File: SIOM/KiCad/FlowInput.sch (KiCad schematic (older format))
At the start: 11 parts, among them Q301 BSS138, Q302 BSS138

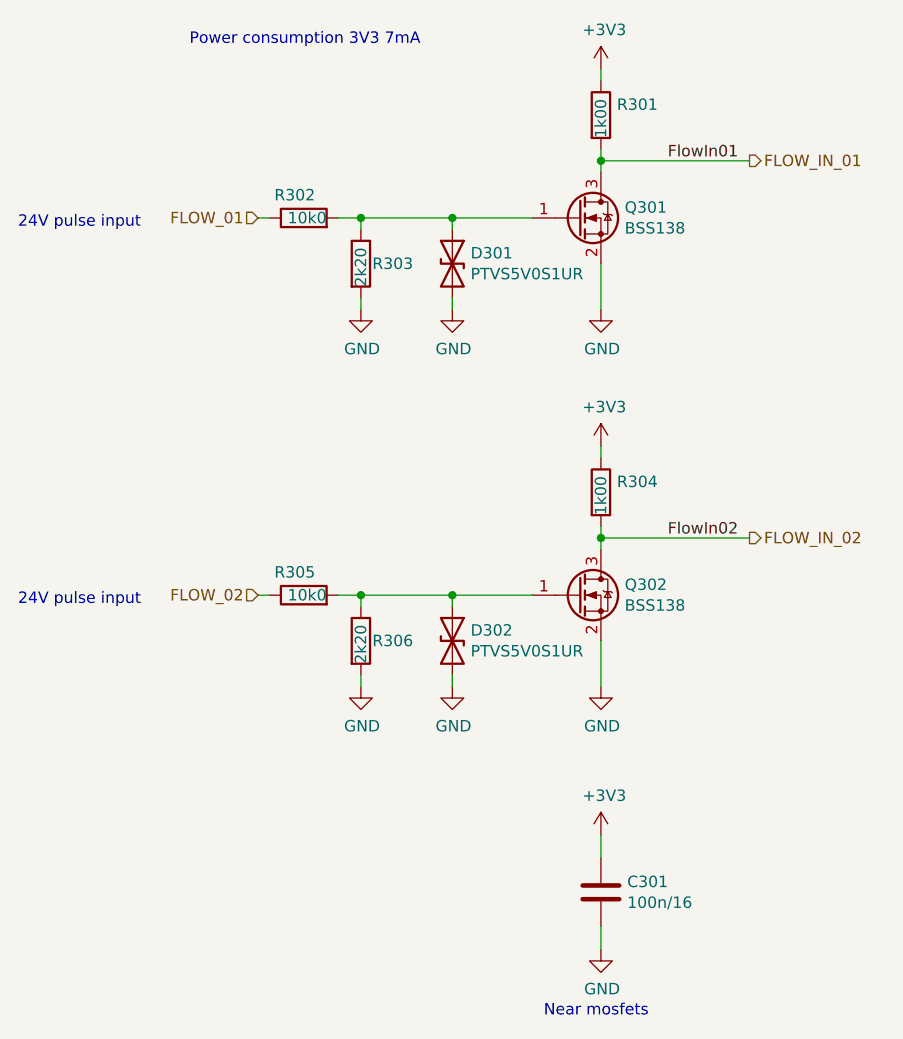
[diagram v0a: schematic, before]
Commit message: KiCad files SIOM_def
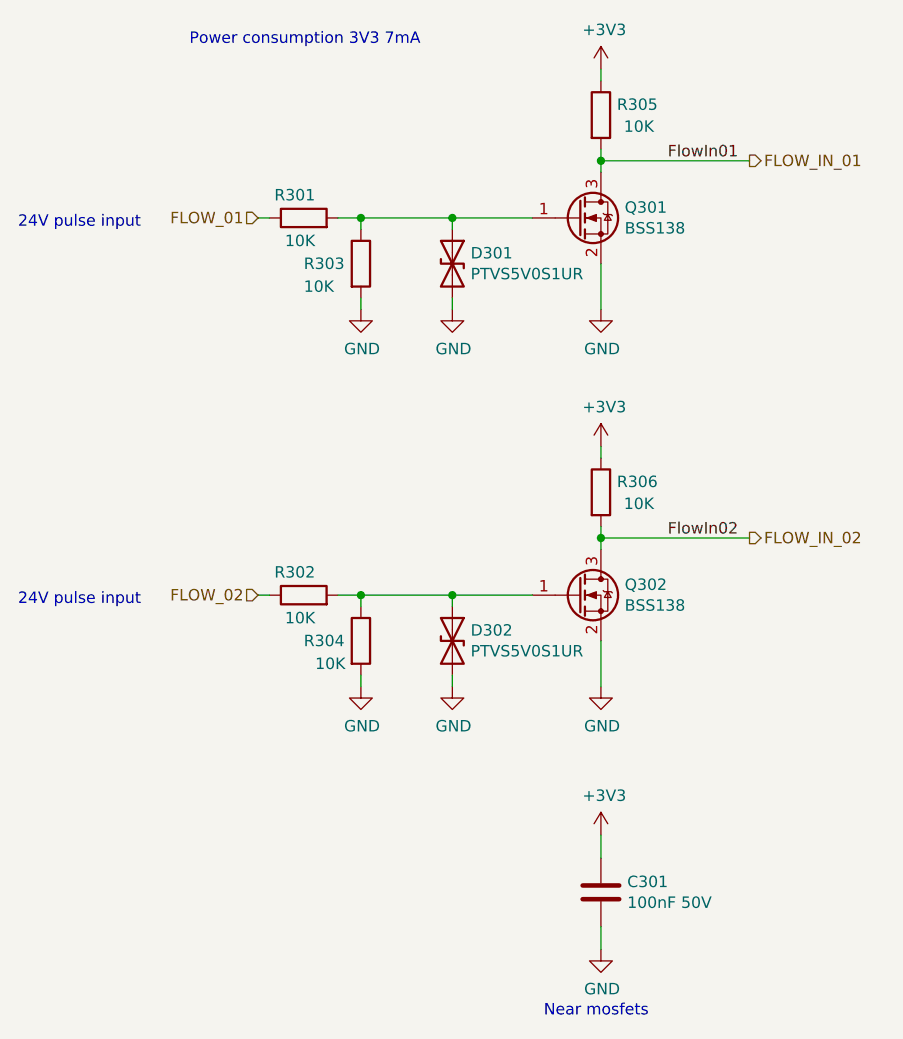
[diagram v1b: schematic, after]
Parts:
- C301: value 100n/16 -> 100nF 50V
- D301, D302: footprint Diode_SMD:Nexperia_CFP3_SOD-123W -> Diode_SMD:D_SOD-123
- R301: renamed from R302; value 10k0 -> 10K
- R302: renamed from R305; value 10k0 -> 10K
- R303: value 2k20 -> 10K
- R304: renamed from R306; value 2k20 -> 10K
- R305: renamed from R301; value 1k00 -> 10K
- R306: renamed from R304; value 1k00 -> 10K
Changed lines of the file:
@@
 EESchema Schematic File Version 4
-LIBS:SIOMv01-cache
 EELAYER 30 0
 EELAYER END
 $Descr A4 11693 8268
 encoding utf-8
-Sheet 3 9
+Sheet 3 10
 Title ""
 Date ""
@@
 AR Path="/5F8BACBE/5FBAA90B" Ref="R?"  Part="1"
 AR Path="/5F8C2412/5FBAA90B" Ref="R303"  Part="1"
-F 0 "R303" H 5300 2600 50  0000 L CNN
-F 1 "2k20" V 5250 2500 50  0000 L CNN
+F 0 "R303" H 5000 2600 50  0000 L CNN
+F 1 "10K" H 5000 2500 50  0000 L CNN
 F 2 "Resistor_SMD:R_0603_1608Metric" V 5180 2600 50  0001 C CNN
 F 3 "~" H 5250 2600 50  0001 C CNN
@@
 AR Path="/5FBAA911" Ref="R?"  Part="1"
 AR Path="/5F8BACBE/5FBAA911" Ref="R?"  Part="1"
-AR Path="/5F8C2412/5FBAA911" Ref="R302"  Part="1"
-F 0 "R302" V 5100 2350 50  0000 L CNN
-F 1 "10k0" V 5000 2300 50  0000 L CNN
+AR Path="/5F8C2412/5FBAA911" Ref="R301"  Part="1"
+F 0 "R301" V 5100 2350 50  0000 L CNN
+F 1 "10K" V 4900 2350 50  0000 L CNN
 F 2 "Resistor_SMD:R_0603_1608Metric" V 4930 2400 50  0001 C CNN
 F 3 "~" H 5000 2400 50  0001 C CNN
@@
 AR Path="/5FBAA93C" Ref="#PWR?"  Part="1"
 AR Path="/5F8BACBE/5FBAA93C" Ref="#PWR?"  Part="1"
-AR Path="/5F8C2412/5FBAA93C" Ref="#PWR0304"  Part="1"
-F 0 "#PWR0304" H 6300 2550 50  0001 C CNN
+AR Path="/5F8C2412/5FBAA93C" Ref="#PWR0306"  Part="1"
+F 0 "#PWR0306" H 6300 2550 50  0001 C CNN
 F 1 "GND" H 6305 2627 50  0000 C CNN
 F 2 "" H 6300 2800 50  0001 C CNN
@@
 F 0 "D301" V 5604 2680 50  0000 L CNN
 F 1 "PTVS5V0S1UR" V 5695 2680 50  0000 L CNN
-F 2 "Diode_SMD:Nexperia_CFP3_SOD-123W" H 5650 2600 50  0001 C CNN
+F 2 "Diode_SMD:D_SOD-123" H 5650 2600 50  0001 C CNN
 F 3 "~" H 5650 2600 50  0001 C CNN
 	1    5650 2600
@@
 AR Path="/5FBBCB25" Ref="#PWR?"  Part="1"
 AR Path="/5F8BACBE/5FBBCB25" Ref="#PWR?"  Part="1"
-AR Path="/5F8C2412/5FBBCB25" Ref="#PWR0302"  Part="1"
-F 0 "#PWR0302" H 5250 2550 50  0001 C CNN
+AR Path="/5F8C2412/5FBBCB25" Ref="#PWR0301"  Part="1"
+F 0 "#PWR0301" H 5250 2550 50  0001 C CNN
 F 1 "GND" H 5255 2627 50  0000 C CNN
 F 2 "" H 5250 2800 50  0001 C CNN
@@
 AR Path="/5FBAA94F" Ref="R?"  Part="1"
 AR Path="/5F8BACBE/5FBAA94F" Ref="R?"  Part="1"
-AR Path="/5F8C2412/5FBAA94F" Ref="R301"  Part="1"
-F 0 "R301" H 6370 1996 50  0000 L CNN
-F 1 "1k00" V 6300 1850 50  0000 L CNN
+AR Path="/5F8C2412/5FBAA94F" Ref="R305"  Part="1"
+F 0 "R305" H 6370 1996 50  0000 L CNN
+F 1 "10K" H 6400 1900 50  0000 L CNN
 F 2 "Resistor_SMD:R_0603_1608Metric" V 6230 1950 50  0001 C CNN
 F 3 "~" H 6300 1950 50  0001 C CNN
@@
 AR Path="/5FBD6639" Ref="R?"  Part="1"
 AR Path="/5F8BACBE/5FBD6639" Ref="R?"  Part="1"
-AR Path="/5F8C2412/5FBD6639" Ref="R306"  Part="1"
-F 0 "R306" H 5300 4250 50  0000 L CNN
-F 1 "2k20" V 5250 4150 50  0000 L CNN
+AR Path="/5F8C2412/5FBD6639" Ref="R304"  Part="1"
+F 0 "R304" H 5000 4250 50  0000 L CNN
+F 1 "10K" H 5050 4150 50  0000 L CNN
 F 2 "Resistor_SMD:R_0603_1608Metric" V 5180 4250 50  0001 C CNN
 F 3 "~" H 5250 4250 50  0001 C CNN
@@
 AR Path="/5FBD663F" Ref="R?"  Part="1"
 AR Path="/5F8BACBE/5FBD663F" Ref="R?"  Part="1"
-AR Path="/5F8C2412/5FBD663F" Ref="R305"  Part="1"
-F 0 "R305" V 5100 4000 50  0000 L CNN
-F 1 "10k0" V 5000 3950 50  0000 L CNN
+AR Path="/5F8C2412/5FBD663F" Ref="R302"  Part="1"
+F 0 "R302" V 5100 4000 50  0000 L CNN
+F 1 "10K" V 4900 4000 50  0000 L CNN
 F 2 "Resistor_SMD:R_0603_1608Metric" V 4930 4050 50  0001 C CNN
 F 3 "~" H 5000 4050 50  0001 C CNN
@@
 AR Path="/5FBD6645" Ref="#PWR?"  Part="1"
 AR Path="/5F8BACBE/5FBD6645" Ref="#PWR?"  Part="1"
-AR Path="/5F8C2412/5FBD6645" Ref="#PWR0307"  Part="1"
-F 0 "#PWR0307" H 5650 4200 50  0001 C CNN
+AR Path="/5F8C2412/5FBD6645" Ref="#PWR0304"  Part="1"
+F 0 "#PWR0304" H 5650 4200 50  0001 C CNN
 F 1 "GND" H 5655 4277 50  0000 C CNN
 F 2 "" H 5650 4450 50  0001 C CNN
@@
 F 0 "D302" V 5604 4330 50  0000 L CNN
 F 1 "PTVS5V0S1UR" V 5695 4330 50  0000 L CNN
-F 2 "Diode_SMD:Nexperia_CFP3_SOD-123W" H 5650 4250 50  0001 C CNN
+F 2 "Diode_SMD:D_SOD-123" H 5650 4250 50  0001 C CNN
 F 3 "~" H 5650 4250 50  0001 C CNN
 	1    5650 4250
@@
 AR Path="/5FBD6667" Ref="#PWR?"  Part="1"
 AR Path="/5F8BACBE/5FBD6667" Ref="#PWR?"  Part="1"
-AR Path="/5F8C2412/5FBD6667" Ref="#PWR0306"  Part="1"
-F 0 "#PWR0306" H 5250 4200 50  0001 C CNN
+AR Path="/5F8C2412/5FBD6667" Ref="#PWR0302"  Part="1"
+F 0 "#PWR0302" H 5250 4200 50  0001 C CNN
 F 1 "GND" H 5255 4277 50  0000 C CNN
 F 2 "" H 5250 4450 50  0001 C CNN
@@
 AR Path="/5FBD667A" Ref="R?"  Part="1"
 AR Path="/5F8BACBE/5FBD667A" Ref="R?"  Part="1"
-AR Path="/5F8C2412/5FBD667A" Ref="R304"  Part="1"
-F 0 "R304" H 6370 3646 50  0000 L CNN
-F 1 "1k00" V 6300 3500 50  0000 L CNN
+AR Path="/5F8C2412/5FBD667A" Ref="R306"  Part="1"
+F 0 "R306" H 6370 3646 50  0000 L CNN
+F 1 "10K" H 6400 3550 50  0000 L CNN
 F 2 "Resistor_SMD:R_0603_1608Metric" V 6230 3600 50  0001 C CNN
 F 3 "~" H 6300 3600 50  0001 C CNN
@@
 P 6300 3400
 AR Path="/5F8BACBE/5FBDD20B" Ref="#PWR?"  Part="1"
-AR Path="/5F8C2412/5FBDD20B" Ref="#PWR0305"  Part="1"
-F 0 "#PWR0305" H 6300 3250 50  0001 C CNN
+AR Path="/5F8C2412/5FBDD20B" Ref="#PWR0307"  Part="1"
+F 0 "#PWR0307" H 6300 3250 50  0001 C CNN
 F 1 "+3V3" H 6315 3573 50  0000 C CNN
 F 2 "" H 6300 3400 50  0001 C CNN
@@
 P 6300 1750
 AR Path="/5F8BACBE/5FBDD9D7" Ref="#PWR?"  Part="1"
-AR Path="/5F8C2412/5FBDD9D7" Ref="#PWR0301"  Part="1"
-F 0 "#PWR0301" H 6300 1600 50  0001 C CNN
+AR Path="/5F8C2412/5FBDD9D7" Ref="#PWR0305"  Part="1"
+F 0 "#PWR0305" H 6300 1600 50  0001 C CNN
 F 1 "+3V3" H 6315 1923 50  0000 C CNN
 F 2 "" H 6300 1750 50  0001 C CNN
@@
 AR Path="/5F8C2412/5FDF090B" Ref="C301"  Part="1"
 F 0 "C301" H 6415 5396 50  0000 L CNN
-F 1 "100n/16" H 6415 5305 50  0000 L CNN
+F 1 "100nF 50V" H 6415 5305 50  0000 L CNN
 F 2 "Capacitor_SMD:C_0603_1608Metric" H 6338 5200 50  0001 C CNN
 F 3 "~" H 6300 5350 50  0001 C CNN
